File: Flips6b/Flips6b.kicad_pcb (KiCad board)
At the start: 2 copper layers, 90 x 50 mm, 23 parts, among them CN1 Conn_02x04_Odd_Even, U1 74HCT595, U2 74HCT595, U3 74HC238, U4 74HC238, U5 74LVC1G04

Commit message: some deco
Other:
- board text added: "Flips 6b v0.1 / 2018-11-01 / SRT"
- board text added: "SRT"
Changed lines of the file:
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@@
   (general
     (thickness 1.6)
-    (drawings 45)
+    (drawings 48)
     (tracks 454)
     (zones 0)
@@
     )
   )
+  (gr_text SRT (at 256.54 72.39 90) (layer F.Paste)
+    (effects (font (size 1.5 1.5) (thickness 0.3)))
+  )
+  (gr_text SRT (at 256.54 72.39 90) (layer F.Mask)
+    (effects (font (size 1.5 1.5) (thickness 0.3)))
+  )
+  (gr_text "Flips 6b\nv0.1 / 2018-11-01 / SRT" (at 196.215 104.775) (layer F.SilkS)
+    (effects (font (size 1.5 1.5) (thickness 0.3)) (justify left))
+  )
   (gr_text "Flips 6b" (at 259.715 72.39 90) (layer F.Cu)

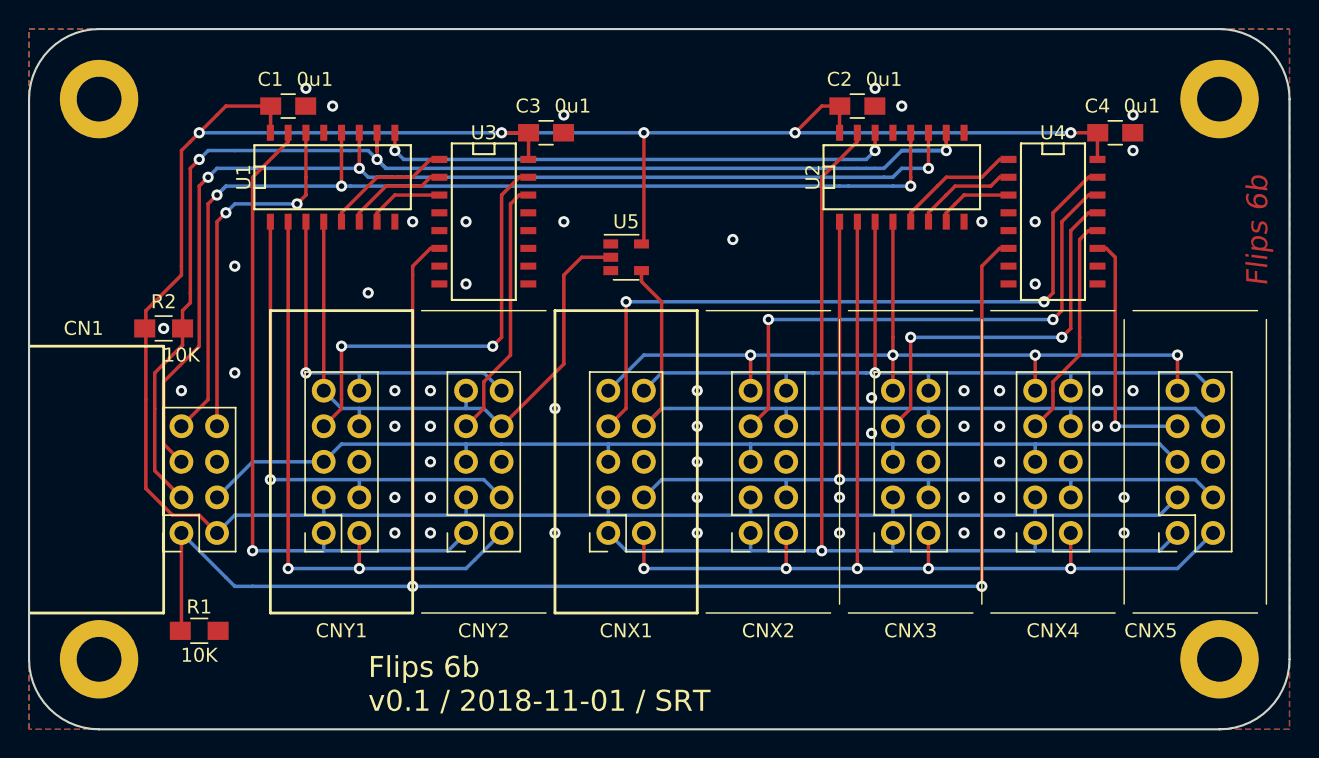
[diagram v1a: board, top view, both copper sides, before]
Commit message: Flips6b use UFP2810 connector
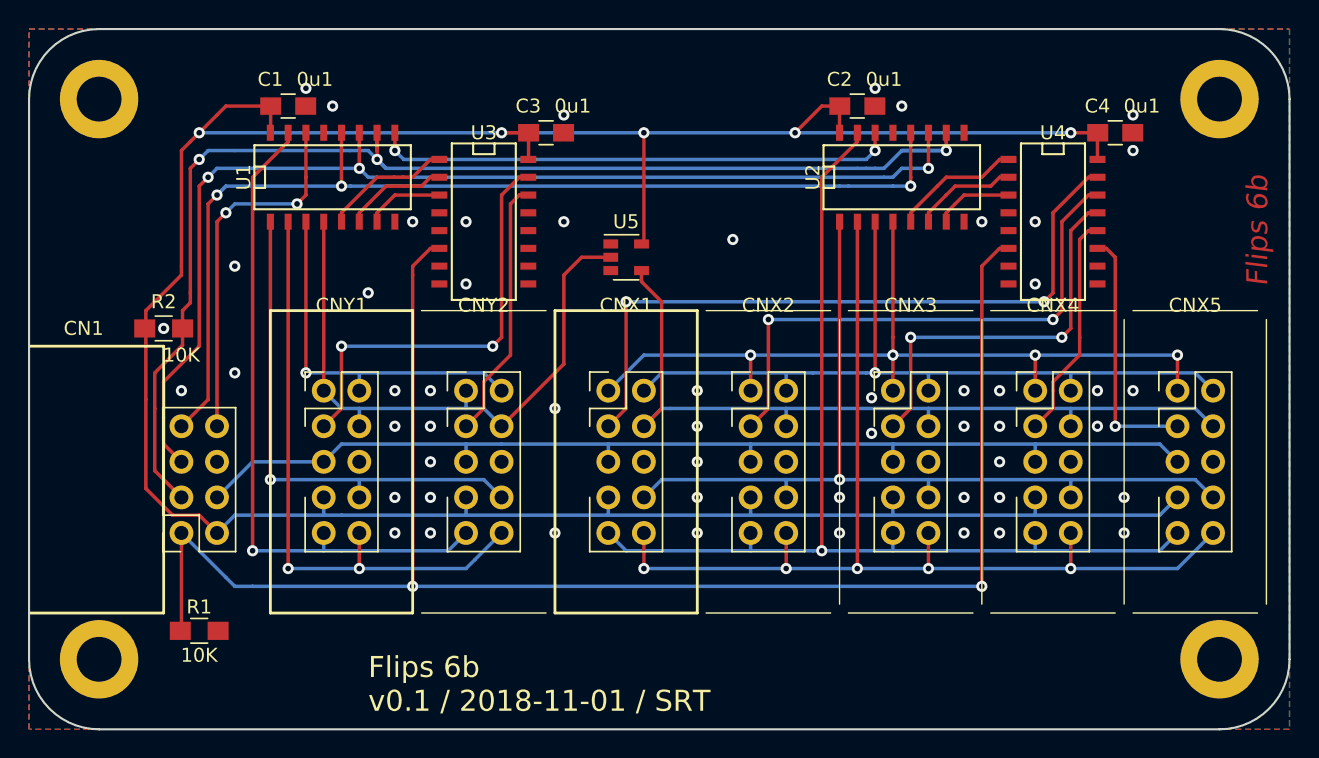
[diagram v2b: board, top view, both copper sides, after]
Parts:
- CNX1, CNX2, CNX3, CNX4, CNX5, CNY1, CNY2: value Conn_02x05_Odd_Even -> UFP2810; footprint Socket_Strips:Socket_Strip_Straight_2x05_Pitch2.54mm -> Own:Pin_Header_Straight_Shrouded_2x05_Pitch2.54mm
- moved CNX1 10.2 mm to (213.4, 83.8), turned to 0 degrees
- moved CNX2 10.2 mm to (223.5, 83.8), turned to 0 degrees
- moved CNX3 10.2 mm to (233.7, 83.8), turned to 0 degrees
- moved CNX4 10.2 mm to (243.8, 83.8), turned to 0 degrees
- moved CNX5 10.2 mm to (254.0, 83.8), turned to 0 degrees
- moved CNY1 10.2 mm to (193.0, 83.8), turned to 0 degrees
- moved CNY2 10.2 mm to (203.2, 83.8), turned to 0 degrees
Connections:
- CNX1 pad 1: /XA0 -> /XB1
- CNX1 pad 10: /XB0 -> /XA2
- CNX1 pad 2: /XA2 -> /XB0
- CNX1 pad 3: +5V -> /XE.0
- CNX1 pad 4: /XA1 -> /XD
- CNX1 pad 7: /XE.0 -> +5V
- CNX1 pad 8: /XD -> /XA1
- CNX1 pad 9: /XB1 -> /XA0
- CNX2 pad 1: /XA0 -> /XB1
- CNX2 pad 10: /XB0 -> /XA2
- CNX2 pad 2: /XA2 -> /XB0
- CNX2 pad 3: +5V -> /XE.1
- CNX2 pad 4: /XA1 -> /XD
- CNX2 pad 7: /XE.1 -> +5V
- CNX2 pad 8: /XD -> /XA1
- CNX2 pad 9: /XB1 -> /XA0
- CNX3 pad 1: /XA0 -> /XB1
- CNX3 pad 10: /XB0 -> /XA2
- CNX3 pad 2: /XA2 -> /XB0
- CNX3 pad 3: +5V -> /XE.2
- CNX3 pad 4: /XA1 -> /XD
- CNX3 pad 7: /XE.2 -> +5V
- CNX3 pad 8: /XD -> /XA1
- CNX3 pad 9: /XB1 -> /XA0
- CNX4 pad 1: /XA0 -> /XB1
- CNX4 pad 10: /XB0 -> /XA2
- CNX4 pad 2: /XA2 -> /XB0
- CNX4 pad 3: +5V -> /XE.3
- CNX4 pad 4: /XA1 -> /XD
- CNX4 pad 7: /XE.3 -> +5V
- CNX4 pad 8: /XD -> /XA1
- CNX4 pad 9: /XB1 -> /XA0
- CNX5 pad 1: /XA0 -> /XB1
- CNX5 pad 10: /XB0 -> /XA2
- CNX5 pad 2: /XA2 -> /XB0
- CNX5 pad 3: +5V -> /XE.4
- CNX5 pad 4: /XA1 -> /XD
- CNX5 pad 7: /XE.4 -> +5V
- CNX5 pad 8: /XD -> /XA1
- CNX5 pad 9: /XB1 -> /XA0
- CNY1 pad 1: /YA0 -> /POL
- CNY1 pad 10: /YB0 -> /YA2
- CNY1 pad 2: /YA2 -> /YB0
- CNY1 pad 3: +5V -> /YE.0
- CNY1 pad 4: /YA1 -> /POL
- CNY1 pad 7: /YE.0 -> +5V
- CNY1 pad 8: /POL -> /YA1
- CNY1 pad 9: /POL -> /YA0
- CNY2 pad 1: /YA0 -> /POL
- CNY2 pad 10: /YB0 -> /YA2
- CNY2 pad 2: /YA2 -> /YB0
- CNY2 pad 3: +5V -> /YE.1
- CNY2 pad 4: /YA1 -> /POL
- CNY2 pad 7: /YE.1 -> +5V
- CNY2 pad 8: /POL -> /YA1
- CNY2 pad 9: /POL -> /YA0
- U2 pad 9: (no net) -> Net-(U2-Pad9)
- U3 pad 10: (no net) -> /YE.5
- U3 pad 11: (no net) -> /YE.4
- U3 pad 7: (no net) -> /YE.7
- U3 pad 9: (no net) -> /YE.6
- U4 pad 10: (no net) -> /XE.5
- U4 pad 7: (no net) -> /XE.7
- U4 pad 9: (no net) -> /XE.6
